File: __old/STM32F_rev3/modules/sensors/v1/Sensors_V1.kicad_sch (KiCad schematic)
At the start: 12 parts, among them J1 Conn_01x05_Female, U1 LM321, U2 LM321

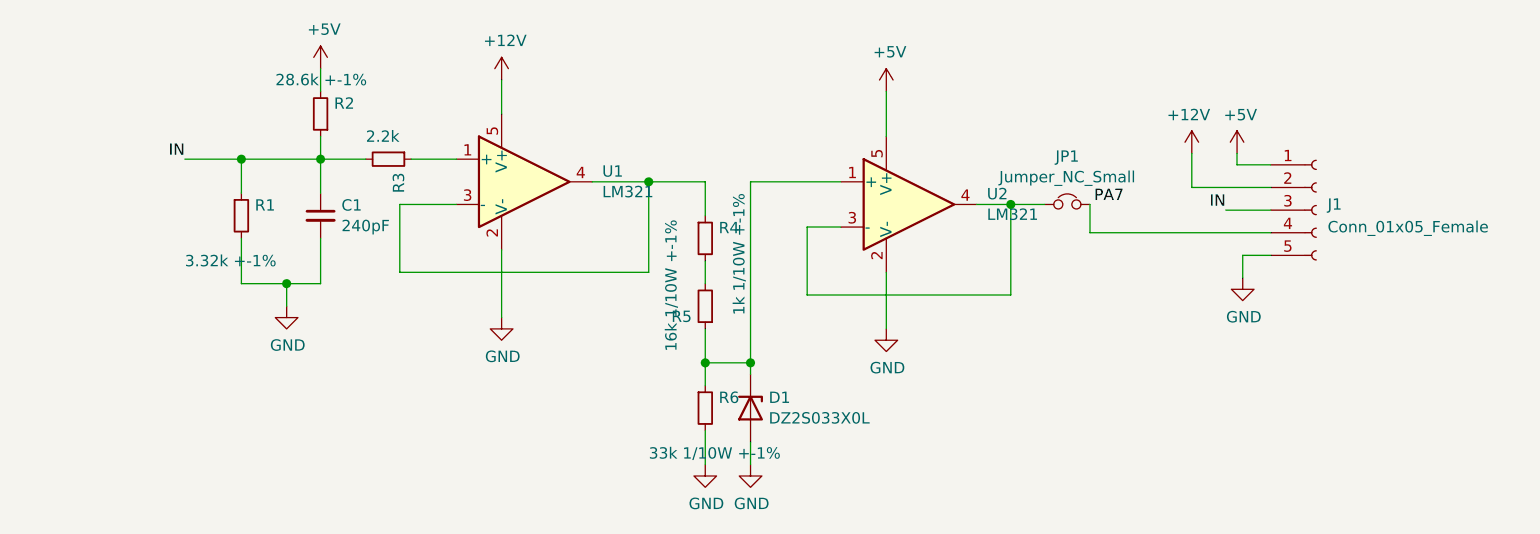
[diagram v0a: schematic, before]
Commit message: move old boards to __old
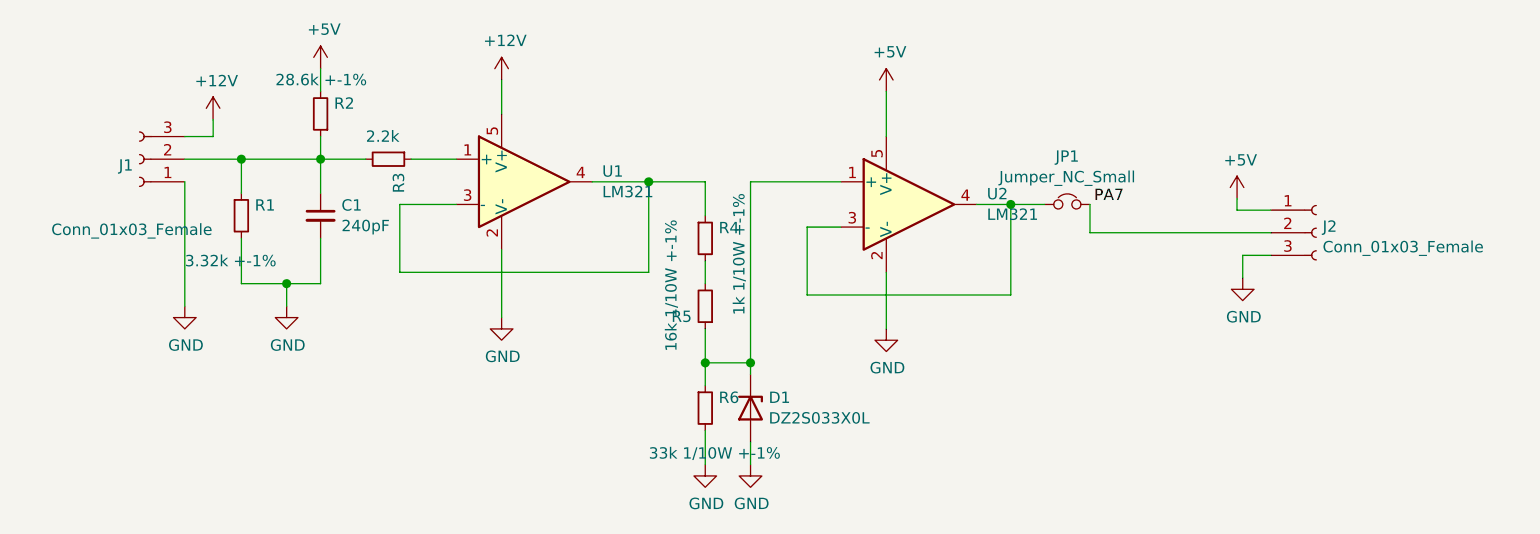
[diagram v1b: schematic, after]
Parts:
- removed J1: Conn_01x05_Female, Connector_PinHeader_1.27mm:PinHeader_1x05_P1.27mm_Horizontal, symbol Connector:Conn_01x05_Female
- added J1, J2: Conn_01x03_Female, Connector_Molex:Molex_PicoBlade_53047-0310_1x03_P1.25mm_Vertical, symbol Connector:Conn_01x03_Female
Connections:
- net +12V: now also J1.3 (Pin_3)
- net +5V: now also J2.1 (Pin_1)
- net GND: now also J1.1 (Pin_1), J2.3 (Pin_3)
- net at JP1.2: now also J2.2 (Pin_2)
- net IN: no longer names the net of C1.1, R1.1, R2.1, R3.2
- net IN: now also J1.2 (Pin_2)
